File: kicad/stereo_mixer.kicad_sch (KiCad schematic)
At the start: 15 parts, among them J101 DC In, J102 Output, J103 Input CH1, J104 Input CH2, J105 Input CH3, J106 Input CH4/5, SW101 Power, U101 LM317L_SO8

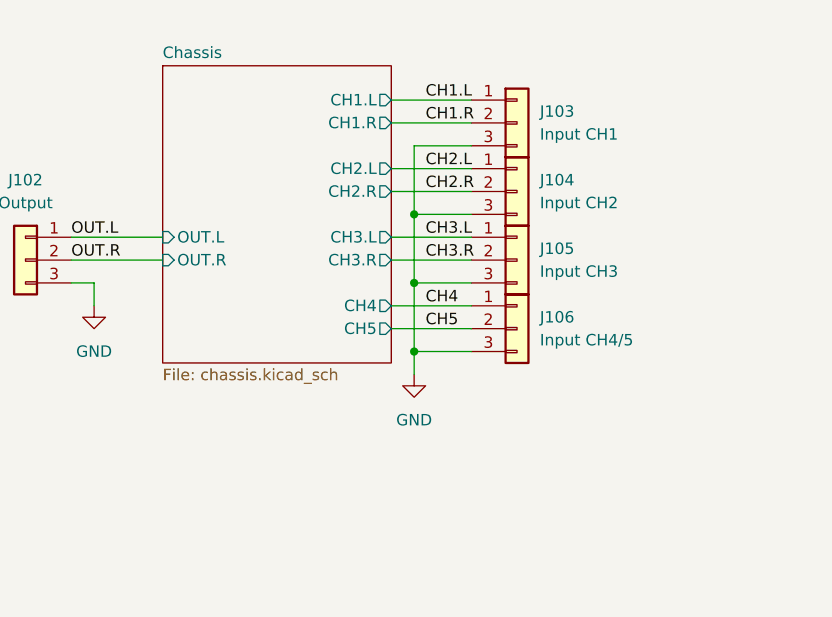
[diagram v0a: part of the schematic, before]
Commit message: split ch4 and ch5 connectors, update footprints
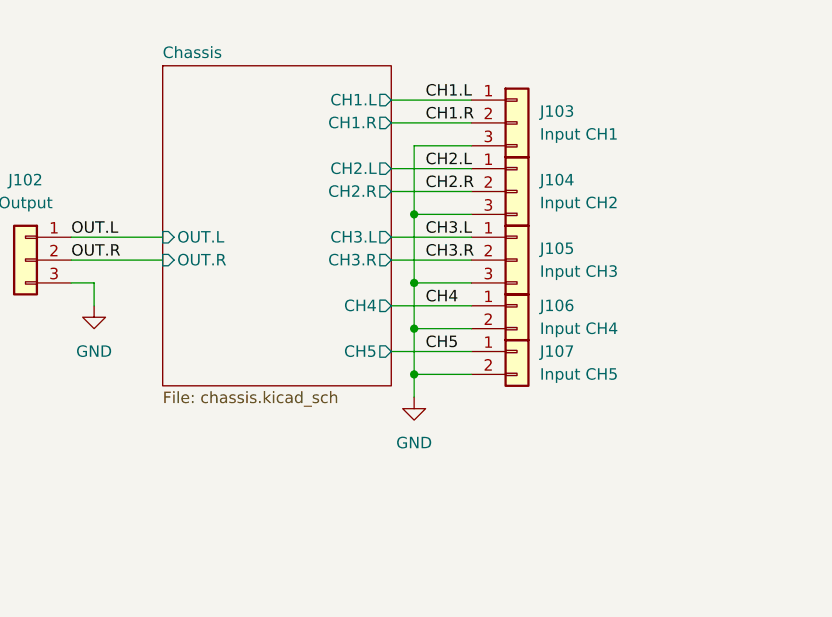
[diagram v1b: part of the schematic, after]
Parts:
- removed J106: Input CH4/5, Connector_Wire:SolderWire-0.25sqmm_1x03_P4.2mm_D0.65mm_OD1.7mm, symbol Connector_Generic:Conn_01x03
- added J106: Input CH4, Custom:ChassisMount_Wire-0.25sqmm_1x02_P4.2mm_D0.65mm_OD1.7mm_1_1, symbol Connector_Generic:Conn_01x02
- added J107: Input CH5, Custom:ChassisMount_Wire-0.25sqmm_1x02_P4.2mm_D0.65mm_OD1.7mm_1_1, symbol Connector_Generic:Conn_01x02
- J102, J103, J104, J105: footprint Connector_Wire:SolderWire-0.25sqmm_1x03_P4.2mm_D0.65mm_OD1.7mm -> Custom:ChassisMount_Wire-0.25sqmm_1x03_P4.2mm_D0.65mm_OD1.7mm_1
- SW101: footprint Connector_Wire:SolderWire-0.5sqmm_1x02_P4.6mm_D0.9mm_OD2.1mm -> Custom:ChassisMount_Wire-0.25sqmm_1x02_P4.2mm_D0.65mm_OD1.7mm_1_1
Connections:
- net CH4: now also J106.1 (Pin_1)
- net CH5: now also J107.1 (Pin_1)
- net GND: now also J106.2 (Pin_2), J107.2 (Pin_2)
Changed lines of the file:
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@@
 	)
 	(junction
-		(at 73.66 63.5)
+		(at 73.66 66.04)
 		(diameter 0)
 		(color 0 0 0 0)
@@
 	)
 	(junction
+		(at 73.66 60.96)
+		(diameter 0)
+		(color 0 0 0 0)
+	)
+	(junction
 		(at 57.15 173.99)
 		(diameter 0)
@@
 	(wire
 		(pts
-			(xy 73.66 55.88) (xy 73.66 63.5)
-		)
-		(stroke
-			(width 0)
-			(type default)
-		)
-	)
-	(wire
-		(pts
-			(xy 73.66 66.04) (xy 73.66 63.5)
+			(xy 73.66 55.88) (xy 73.66 60.96)
+		)
+		(stroke
+			(width 0)
+			(type default)
+		)
+	)
+	(wire
+		(pts
+			(xy 71.12 63.5) (xy 80.01 63.5)
 		)
 		(stroke
@@
 	(wire
 		(pts
+			(xy 73.66 68.58) (xy 73.66 66.04)
+		)
+		(stroke
+			(width 0)
+			(type default)
+		)
+	)
+	(wire
+		(pts
 			(xy 57.15 186.69) (xy 35.56 186.69)
 		)
@@
 	(wire
 		(pts
+			(xy 73.66 66.04) (xy 80.01 66.04)
+		)
+		(stroke
+			(width 0)
+			(type default)
+		)
+	)
+	(wire
+		(pts
 			(xy 35.56 50.8) (xy 45.72 50.8)
 		)
@@
 	(wire
 		(pts
+			(xy 73.66 60.96) (xy 73.66 66.04)
+		)
+		(stroke
+			(width 0)
+			(type default)
+		)
+	)
+	(wire
+		(pts
 			(xy 167.64 62.23) (xy 170.18 62.23)
 		)
@@
 	(wire
 		(pts
-			(xy 73.66 63.5) (xy 80.01 63.5)
-		)
-		(stroke
-			(width 0)
-			(type default)
-		)
-	)
-	(wire
-		(pts
 			(xy 224.79 156.21) (xy 224.79 158.75)
 		)
@@
 	(wire
 		(pts
-			(xy 71.12 60.96) (xy 80.01 60.96)
-		)
-		(stroke
-			(width 0)
-			(type default)
-		)
-	)
-	(wire
-		(pts
 			(xy 90.17 177.8) (xy 92.71 177.8)
 		)
@@
 		(pts
 			(xy 35.56 55.88) (xy 38.1 55.88)
+		)
+		(stroke
+			(width 0)
+			(type default)
+		)
+	)
+	(wire
+		(pts
+			(xy 73.66 60.96) (xy 80.01 60.96)
 		)
 		(stroke
@@
 	)
 	(label "CH5"
-		(at 74.93 60.96 0)
+		(at 74.93 63.5 0)
 		(effects
 			(font
@@
 			)
 		)
-		(property "Footprint" "Connector_Wire:SolderWire-0.25sqmm_1x03_P4.2mm_D0.65mm_OD1.7mm"
+		(property "Footprint" "Custom:ChassisMount_Wire-0.25sqmm_1x03_P4.2mm_D0.65mm_OD1.7mm_1"
 			(at 85.09 53.34 0)
 			(effects
@@
 			)
 		)
-		(property "Footprint" "Connector_Wire:SolderWire-0.25sqmm_1x03_P4.2mm_D0.65mm_OD1.7mm"
+		(property "Footprint" "Custom:ChassisMount_Wire-0.25sqmm_1x03_P4.2mm_D0.65mm_OD1.7mm_1"
 			(at 30.48 53.34 0)
 			(effects
@@
 			)
 		)
-		(property "Footprint" "Connector_Wire:SolderWire-0.25sqmm_1x03_P4.2mm_D0.65mm_OD1.7mm"
+		(property "Footprint" "Custom:ChassisMount_Wire-0.25sqmm_1x03_P4.2mm_D0.65mm_OD1.7mm_1"
 			(at 85.09 38.1 0)
 			(effects
@@
 			)
 		)
-		(property "Footprint" "Connector_Wire:SolderWire-0.5sqmm_1x02_P4.6mm_D0.9mm_OD2.1mm"
+		(property "Footprint" "Custom:ChassisMount_Wire-0.25sqmm_1x02_P4.2mm_D0.65mm_OD1.7mm_1_1"
 			(at 45.72 173.99 0)
 			(effects
@@
 				(path "/cf7176a5-9cff-4e58-aeea-84be54604336"
 					(reference "SW101")
+					(unit 1)
+				)
+			)
+		)
+	)
+	(symbol
+		(lib_id "Connector_Generic:Conn_01x02")
+		(at 85.09 58.42 0)
+		(unit 1)
+		(exclude_from_sim no)
+		(in_bom no)
+		(on_board yes)
+		(dnp no)
+		(fields_autoplaced yes)
+		(property "Reference" "J106"
+			(at 87.63 58.4199 0)
+			(effects
+				(font
+					(size 1.27 1.27)
+				)
+				(justify left)
+			)
+		)
+		(property "Value" "Input CH4"
+			(at 87.63 60.9599 0)
+			(effects
+				(font
+					(size 1.27 1.27)
+				)
+				(justify left)
+			)
+		)
+		(property "Footprint" "Custom:ChassisMount_Wire-0.25sqmm_1x02_P4.2mm_D0.65mm_OD1.7mm_1_1"
+			(at 85.09 58.42 0)
+			(effects
+				(font
+					(size 1.27 1.27)
+				)
+				(hide yes)
+			)
+		)
+		(property "Datasheet" "~"
+			(at 85.09 58.42 0)
+			(effects
+				(font
+					(size 1.27 1.27)
+				)
+				(hide yes)
+			)
+		)
+		(property "Description" "Generic connector, single row, 01x02, script generated (kicad-library-utils/schlib/autogen/connector/)"
+			(at 85.09 58.42 0)
+			(effects
+				(font
+					(size 1.27 1.27)
+				)
+				(hide yes)
+			)
+		)
+		(property "Supplier" "N/A"
+			(at 85.09 58.42 0)
+			(effects
+				(font
+					(size 1.27 1.27)
+				)
+				(hide yes)
+			)
+		)
+		(pin "1"
+		)
+		(pin "2"
+		)
+		(instances
+			(project ""
+				(path "/cf7176a5-9cff-4e58-aeea-84be54604336"
+					(reference "J106")
 					(unit 1)
 				)
@@
 			)
 		)
-		(property "Footprint" "Connector_Wire:SolderWire-0.25sqmm_1x03_P4.2mm_D0.65mm_OD1.7mm"
+		(property "Footprint" "Custom:ChassisMount_Wire-0.25sqmm_1x03_P4.2mm_D0.65mm_OD1.7mm_1"
 			(at 85.09 45.72 0)
 			(effects
@@
 				(path "/cf7176a5-9cff-4e58-aeea-84be54604336"
 					(reference "J104")
-					(unit 1)
-				)
-			)
-		)
-	)
-	(symbol
-		(lib_id "Connector_Generic:Conn_01x03")
-		(at 85.09 60.96 0)
-		(unit 1)
-		(exclude_from_sim no)
-		(in_bom no)
-		(on_board yes)
-		(dnp no)
-		(fields_autoplaced yes)
-		(property "Reference" "J106"
-			(at 87.63 59.6899 0)
-			(effects
-				(font
-					(size 1.27 1.27)
-				)
-				(justify left)
-			)
-		)
-		(property "Value" "Input CH4/5"
-			(at 87.63 62.2299 0)
-			(effects
-				(font
-					(size 1.27 1.27)
-				)
-				(justify left)
-			)
-		)
-		(property "Footprint" "Connector_Wire:SolderWire-0.25sqmm_1x03_P4.2mm_D0.65mm_OD1.7mm"
-			(at 85.09 60.96 0)
-			(effects
-				(font
-					(size 1.27 1.27)
-				)
-				(hide yes)
-			)
-		)
-		(property "Datasheet" "~"
-			(at 85.09 60.96 0)
-			(effects
-				(font
-					(size 1.27 1.27)
-				)
-				(hide yes)
-			)
-		)
-		(property "Description" "Generic connector, single row, 01x03, script generated (kicad-library-utils/schlib/autogen/connector/)"
-			(at 85.09 60.96 0)
-			(effects
-				(font
-					(size 1.27 1.27)
-				)
-				(hide yes)
-			)
-		)
-		(property "Supplier" "N/A"
-			(at 85.09 60.96 0)
-			(effects
-				(font
-					(size 1.27 1.27)
-				)
-				(hide yes)
-			)
-		)
-		(pin "2"
-		)
-		(pin "1"
-		)
-		(pin "3"
-		)
-		(instances
-			(project "stereo_mixer"
-				(path "/cf7176a5-9cff-4e58-aeea-84be54604336"
-					(reference "J106")
 					(unit 1)
 				)
@@
 	(symbol
 		(lib_id "power:GND")
-		(at 73.66 66.04 0)
+		(at 73.66 68.58 0)
 		(unit 1)
 		(exclude_from_sim no)
@@
 		(fields_autoplaced yes)
 		(property "Reference" "#PWR0104"
-			(at 73.66 72.39 0)
+			(at 73.66 74.93 0)
 			(effects
 				(font
@@
 		)
 		(property "Value" "GND"
-			(at 73.66 71.12 0)
+			(at 73.66 73.66 0)
 			(effects
 				(font
@@
 		)
 		(property "Footprint" ""
-			(at 73.66 66.04 0)
+			(at 73.66 68.58 0)
 			(effects
 				(font
@@
 		)
 		(property "Datasheet" ""
-			(at 73.66 66.04 0)
+			(at 73.66 68.58 0)
 			(effects
 				(font
@@
 		)
 		(property "Description" "Power symbol creates a global label with name \"GND\" , ground"
-			(at 73.66 66.04 0)
+			(at 73.66 68.58 0)
 			(effects
 				(font
@@
 				(path "/cf7176a5-9cff-4e58-aeea-84be54604336"
 					(reference "#PWR0104")
+					(unit 1)
+				)
+			)
+		)
+	)
+	(symbol
+		(lib_id "Connector_Generic:Conn_01x02")
+		(at 85.09 63.5 0)
+		(unit 1)
+		(exclude_from_sim no)
+		(in_bom no)
+		(on_board yes)
+		(dnp no)
+		(fields_autoplaced yes)
+		(property "Reference" "J107"
+			(at 87.63 63.4999 0)
+			(effects
+				(font
+					(size 1.27 1.27)
+				)
+				(justify left)
+			)
+		)
+		(property "Value" "Input CH5"
+			(at 87.63 66.0399 0)
+			(effects
+				(font
+					(size 1.27 1.27)
+				)
+				(justify left)
+			)
+		)
+		(property "Footprint" "Custom:ChassisMount_Wire-0.25sqmm_1x02_P4.2mm_D0.65mm_OD1.7mm_1_1"
+			(at 85.09 63.5 0)
+			(effects
+				(font
+					(size 1.27 1.27)
+				)
+				(hide yes)
+			)
+		)
+		(property "Datasheet" "~"
+			(at 85.09 63.5 0)
+			(effects
+				(font
+					(size 1.27 1.27)
+				)
+				(hide yes)
+			)
+		)
+		(property "Description" "Generic connector, single row, 01x02, script generated (kicad-library-utils/schlib/autogen/connector/)"
+			(at 85.09 63.5 0)
+			(effects
+				(font
+					(size 1.27 1.27)
+				)
+				(hide yes)
+			)
+		)
+		(property "Supplier" "N/A"
+			(at 85.09 63.5 0)
+			(effects
+				(font
+					(size 1.27 1.27)
+				)
+				(hide yes)
+			)
+		)
+		(pin "1"
+		)
+		(pin "2"
+		)
+		(instances
+			(project "stereo_mixer"
+				(path "/cf7176a5-9cff-4e58-aeea-84be54604336"
+					(reference "J107")
 					(unit 1)
 				)
@@
 	(sheet
 		(at 45.72 31.75)
-		(size 25.4 33.02)
+		(size 25.4 35.56)
 		(exclude_from_sim no)
 		(in_bom yes)
@@
 		)
 		(property "Sheetfile" "chassis.kicad_sch"
-			(at 45.72 65.3546 0)
+			(at 45.72 67.8946 0)
 			(effects
 				(font
@@
 		)
 		(pin "CH5" output
-			(at 71.12 60.96 0)
-			(effects
-				(font
+			(at 71.12 63.5 0)
+			(effects
+				(font

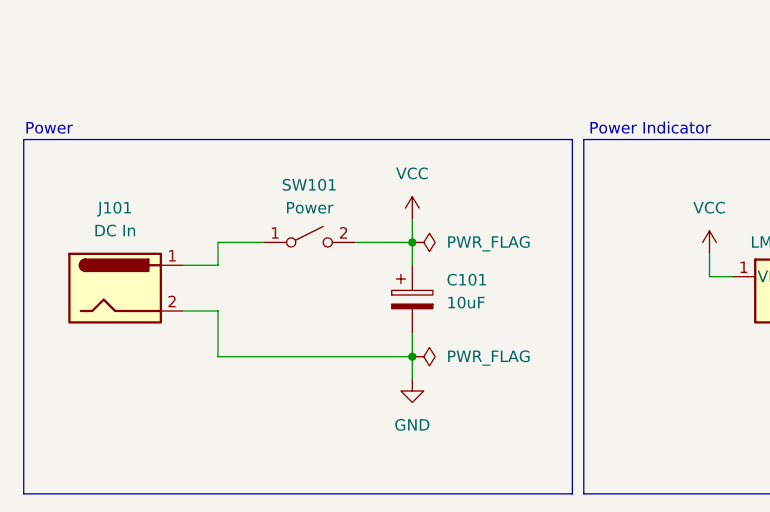
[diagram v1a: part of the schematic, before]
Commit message: replace electrolytic caps with ceramics
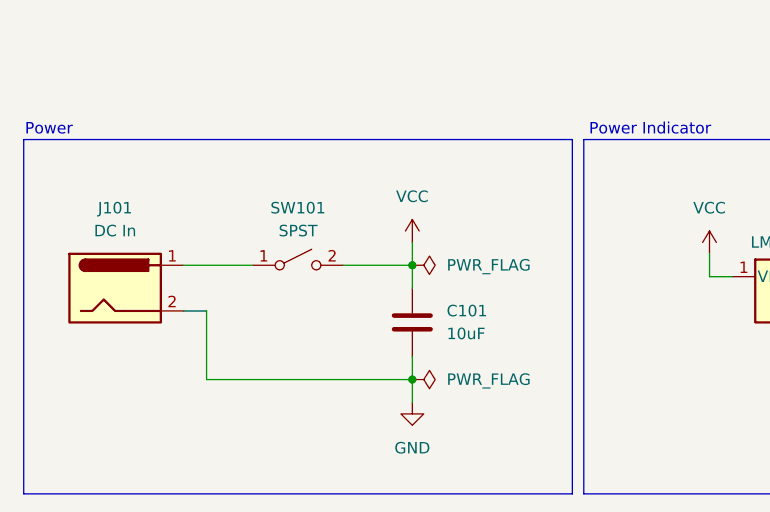
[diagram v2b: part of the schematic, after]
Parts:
- removed C101: 10uF, Capacitor_THT:CP_Radial_D5.0mm_P2.00mm, symbol Device:C_Polarized
- added C101: 10uF, Capacitor_SMD:C_1206_3216Metric, symbol Device:C
- SW101: value Power -> SPST
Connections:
- net GND: now also C101.2
- net VCC: now also C101.1
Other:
- moved on the sheet: SW101

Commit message: fix symbol library links
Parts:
- J102, J103, J104, J105: footprint Custom:ChassisMount_Wire-0.25sqmm_1x03_P4.2mm_D0.65mm_OD1.7mm_1 -> Custom:ChassisMount_Wire-0.25sqmm_1x03_P4.2mm_D0.65mm_OD1.7mm
- J106, J107, SW101: footprint Custom:ChassisMount_Wire-0.25sqmm_1x02_P4.2mm_D0.65mm_OD1.7mm_1_1 -> Custom:ChassisMount_Wire-0.25sqmm_1x02_P4.2mm_D0.65mm_OD1.7mm
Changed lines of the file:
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@@
 			)
 		)
-		(property "Footprint" "Custom:ChassisMount_Wire-0.25sqmm_1x03_P4.2mm_D0.65mm_OD1.7mm_1"
+		(property "Footprint" "Custom:ChassisMount_Wire-0.25sqmm_1x03_P4.2mm_D0.65mm_OD1.7mm"
 			(at 85.09 53.34 0)
 			(effects
@@
 			)
 		)
-		(property "Footprint" "Custom:ChassisMount_Wire-0.25sqmm_1x03_P4.2mm_D0.65mm_OD1.7mm_1"
+		(property "Footprint" "Custom:ChassisMount_Wire-0.25sqmm_1x03_P4.2mm_D0.65mm_OD1.7mm"
 			(at 30.48 53.34 0)
 			(effects
@@
 			)
 		)
-		(property "Footprint" "Custom:ChassisMount_Wire-0.25sqmm_1x03_P4.2mm_D0.65mm_OD1.7mm_1"
+		(property "Footprint" "Custom:ChassisMount_Wire-0.25sqmm_1x03_P4.2mm_D0.65mm_OD1.7mm"
 			(at 85.09 38.1 0)
 			(effects
@@
 			)
 		)
-		(property "Footprint" "Custom:ChassisMount_Wire-0.25sqmm_1x02_P4.2mm_D0.65mm_OD1.7mm_1_1"
+		(property "Footprint" "Custom:ChassisMount_Wire-0.25sqmm_1x02_P4.2mm_D0.65mm_OD1.7mm"
 			(at 44.45 176.53 0)
 			(effects
@@
 			)
 		)
-		(property "Footprint" "Custom:ChassisMount_Wire-0.25sqmm_1x02_P4.2mm_D0.65mm_OD1.7mm_1_1"
+		(property "Footprint" "Custom:ChassisMount_Wire-0.25sqmm_1x02_P4.2mm_D0.65mm_OD1.7mm"
 			(at 85.09 58.42 0)
 			(effects
@@
 			)
 		)
-		(property "Footprint" "Custom:ChassisMount_Wire-0.25sqmm_1x03_P4.2mm_D0.65mm_OD1.7mm_1"
+		(property "Footprint" "Custom:ChassisMount_Wire-0.25sqmm_1x03_P4.2mm_D0.65mm_OD1.7mm"
 			(at 85.09 45.72 0)
 			(effects
@@
 			)
 		)
-		(property "Footprint" "Custom:ChassisMount_Wire-0.25sqmm_1x02_P4.2mm_D0.65mm_OD1.7mm_1_1"
+		(property "Footprint" "Custom:ChassisMount_Wire-0.25sqmm_1x02_P4.2mm_D0.65mm_OD1.7mm"
 			(at 85.09 63.5 0)
 			(effects

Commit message: change led to smt, update schematic rev
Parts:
- D101: value LED -> Green; footprint LED_THT:LED_D5.0mm -> LED_SMD:LED_0603_1608Metric; Supplier Generic -> https://www.digikey.com/en/products/detail/harvatek-corpora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
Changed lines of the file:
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@@
 	(title_block
 		(title "Stereo Mixer")
-		(date "2025-10-30")
-		(rev "1.0")
+		(date "2026-01-08")
+		(rev "1.1")
 		(company "vladaviedov.org")
-		(comment 1 "Power: 12-30V Barrel Jack")
+		(comment 1 "Power: 5-25V Barrel Jack")
 		(comment 2 "CH4-5: Instrument Mono")
 		(comment 3 "CH1-3: Line Stereo")
@@
 		(on_board yes)
 		(dnp no)
-		(fields_autoplaced yes)
 		(property "Reference" "D101"
-			(at 129.54 184.4674 90)
+			(at 129.54 184.404 90)
 			(effects
 				(font
@@
 			)
 		)
-		(property "Value" "LED"
+		(property "Value" "Green"
 			(at 129.54 187.0074 90)
 			(effects
@@
 			)
 		)
-		(property "Footprint" "LED_THT:LED_D5.0mm"
+		(property "Footprint" "LED_SMD:LED_0603_1608Metric"
 			(at 125.73 184.15 0)
 			(effects
@@
 			)
 		)
-		(property "Supplier" "Generic"
+		(property "Supplier" "https://www.digikey.com/en/products/detail/harvatek-corporation/B1911NG-20D000214U1930/15519989"
 			(at 125.73 184.15 90)
 			(effects

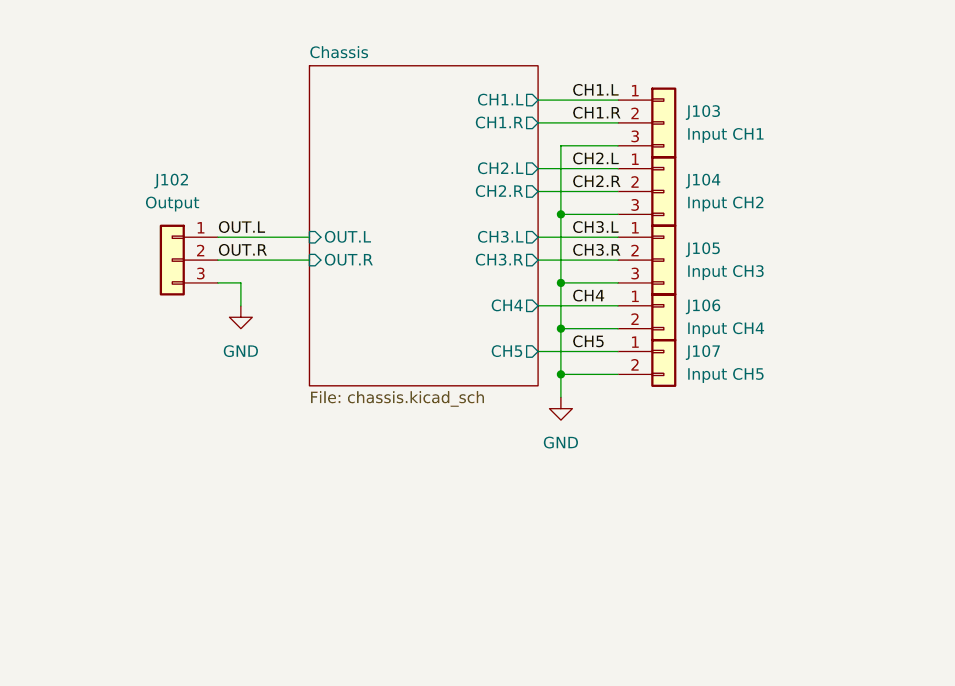
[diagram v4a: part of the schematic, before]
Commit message: modify stereo channel footprints
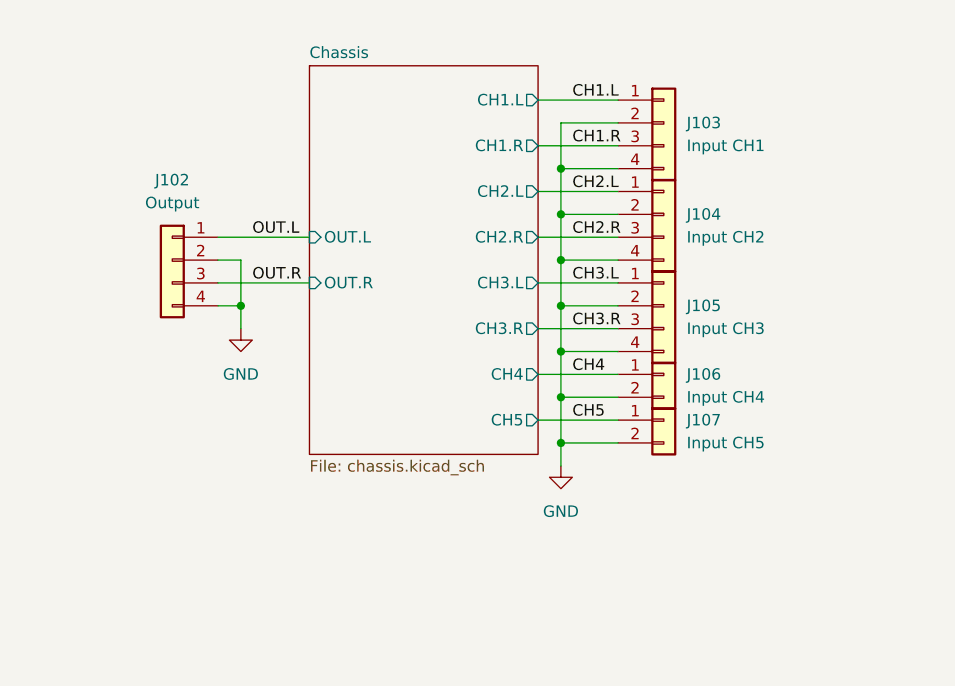
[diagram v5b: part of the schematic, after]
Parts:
- J102, J103, J104, J105: footprint Custom:ChassisMount_Wire-0.25sqmm_1x03_P4.2mm_D0.65mm_OD1.7mm -> Custom:ChassisMount_Wire-0.25sqmm_2x02_P4.2mm_D0.65mm_OD1.7mm; symbol Connector_Generic:Conn_01x03 -> Connector_Generic:Conn_01x04; now in the parts list
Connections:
- net CH1.R: now also J103.3 (Pin_3); no longer J103.2 (Pin_2)
- net CH2.R: now also J104.3 (Pin_3); no longer J104.2 (Pin_2)
- net CH3.R: now also J105.3 (Pin_3); no longer J105.2 (Pin_2)
- net GND: now also J102.2 (Pin_2), J102.4 (Pin_4), J103.2 (Pin_2), J103.4 (Pin_4), J104.2 (Pin_2), J104.4 (Pin_4), J105.2 (Pin_2), J105.4 (Pin_4); no longer J102.3 (Pin_3), J103.3 (Pin_3), J104.3 (Pin_3), J105.3 (Pin_3)
- net OUT.R: now also J102.3 (Pin_3); no longer J102.2 (Pin_2)
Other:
- moved on the sheet: J106, J107
